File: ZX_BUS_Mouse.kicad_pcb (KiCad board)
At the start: 2 copper layers, 99.1 x 40 mm, 28 parts, among them J1 X1A, J2 X1B, J4 Mini-DIN-6, J5 Conn_02x03_Odd_Even ISP, J6 Conn_01x04 Debug, J7 Conn_02x05_Odd_Even JTAG, U1 ATmega8A-A, U2 EPM3032ALC44, U3 AMS1117-3.3

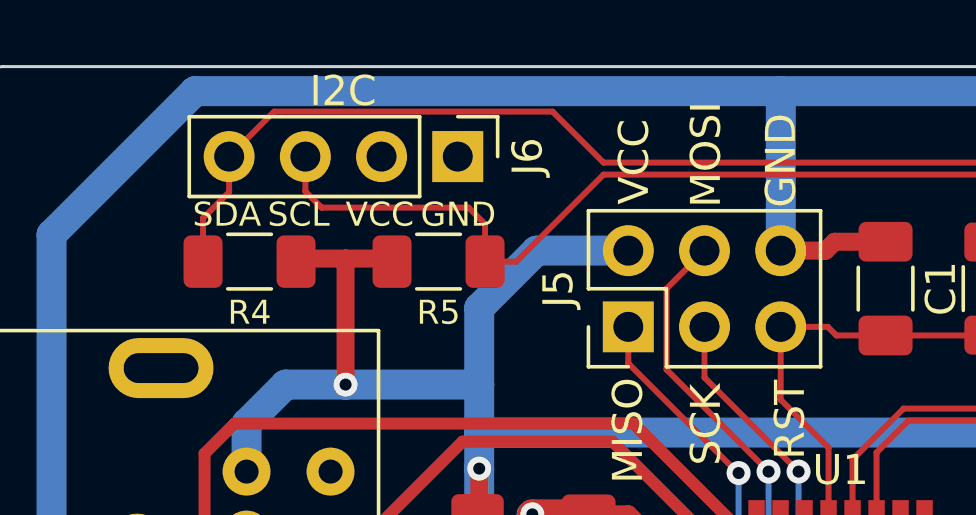
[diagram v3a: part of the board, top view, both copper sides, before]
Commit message: Connect I2C to VCC and GND.
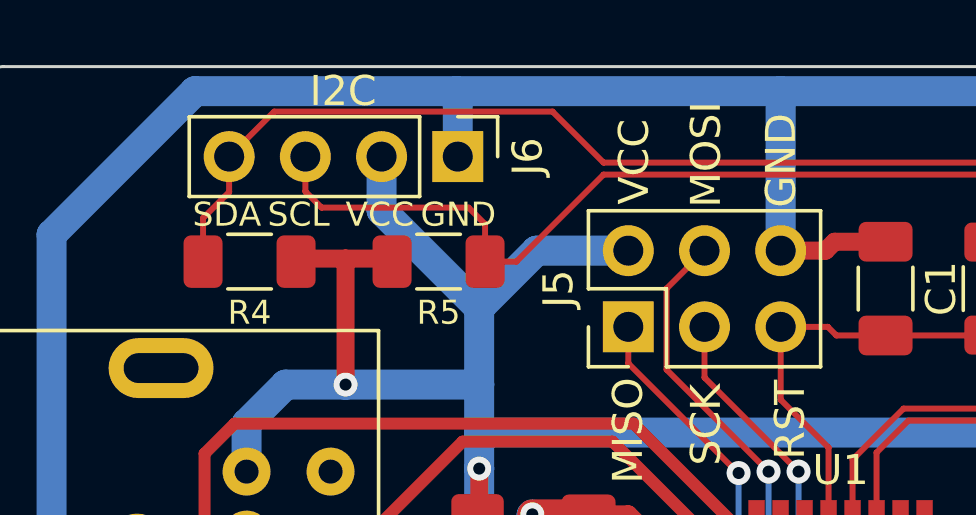
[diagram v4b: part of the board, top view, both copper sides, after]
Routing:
- net VCC: track 138.9 -> 145.3 mm
- net GND: track 497.9 -> 500.0 mm
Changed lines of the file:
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@@
   (via (at 115.2 138.2) (size 0.8) (drill 0.4) (layers "F.Cu" "B.Cu") (net 3))
   (segment (start 63.1 138.2) (end 135 138.2) (width 1) (layer "B.Cu") (net 3))
+  (segment (start 58.34 112.9) (end 58.34 110.75875) (width 1) (layer "B.Cu") (net 3))
   (segment (start 69.105 116.035) (end 69.105 110.72375) (width 1) (layer "B.Cu") (net 3))
   (segment (start 46.5 130.2) (end 51.3 130.2) (width 1) (layer "B.Cu") (net 3))
@@
   (segment (start 69.105 110.72375) (end 69.1 110.71875) (width 1) (layer "B.Cu") (net 3))
   (segment (start 115.18125 135.31875) (end 115.2 135.3) (width 0.6) (layer "B.Cu") (net 3))
+  (segment (start 58.3 110.71875) (end 49.58125 110.71875) (width 1) (layer "B.Cu") (net 3))
   (segment (start 112.4625 134.14125) (end 111.03 132.70875) (width 0.6) (layer "B.Cu") (net 3))
   (segment (start 100.8 130.48125) (end 102.01875 130.48125) (width 0.6) (layer "B.Cu") (net 3))
+  (segment (start 69.1 110.71875) (end 58.3 110.71875) (width 1) (layer "B.Cu") (net 3))
   (segment (start 97.3 132.5) (end 97.3 121.6) (width 1) (layer "B.Cu") (net 3))
   (segment (start 60.8 135.9) (end 63.1 138.2) (width 1) (layer "B.Cu") (net 3))
@@
   (segment (start 116.11 114.01) (end 116.11 114.92875) (width 0.6) (layer "B.Cu") (net 3))
   (segment (start 115.7625 113.6625) (end 116.11 114.01) (width 0.6) (layer "B.Cu") (net 3))
+  (segment (start 58.34 110.75875) (end 58.3 110.71875) (width 1) (layer "B.Cu") (net 3))
   (segment (start 136.31875 110.71875) (end 69.1 110.71875) (width 1) (layer "B.Cu") (net 3))
   (segment (start 122.41875 112.31875) (end 115.7625 112.31875) (width 1) (layer "B.Cu") (net 3))
@@
   (segment (start 112.4625 135.31875) (end 115.18125 135.31875) (width 1) (layer "B.Cu") (net 3))
   (segment (start 137 129.41875) (end 137.6 128.81875) (width 1) (layer "B.Cu") (net 3))
-  (segment (start 69.1 110.71875) (end 49.58125 110.71875) (width 1) (layer "B.Cu") (net 3))
   (segment (start 60.8 124.85) (end 60.8 130.8) (width 1) (layer "B.Cu") (net 3))
   (segment (start 93 118.56875) (end 92.8 118.76875) (width 1) (layer "B.Cu") (net 3))
@@
   (segment (start 81.65 113.55) (end 79.95 115.25) (width 1) (layer "B.Cu") (net 57))
   (segment (start 79.95 122.35) (end 83.3 125.7) (width 1) (layer "B.Cu") (net 57))
+  (segment (start 55.8 114.69) (end 59.055 117.945) (width 1) (layer "B.Cu") (net 57))
   (segment (start 83.3 130.565688) (end 83.282844 130.582844) (width 1) (layer "B.Cu") (net 57))
+  (segment (start 55.8 112.9) (end 55.8 114.69) (width 1) (layer "B.Cu") (net 57))
   (segment (start 64.025 116.035) (end 60.965 116.035) (width 1) (layer "B.Cu") (net 57))
   (segment (start 54.6 120.5) (end 52.6 120.5) (width 1) (layer "B.Cu") (net 57))

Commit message: Add labels to PCB.
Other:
- board text added: "JTAG"
- board text added: "ZX BUS Kempston Mouse Controller"
- board text added: "github.com/proboterror/ZX_BUS_Mouse"
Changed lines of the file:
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@@
     (effects (font (size 1 0.9) (thickness 0.15)) (justify mirror))
+  )
+  (gr_text "ZX BUS Kempston Mouse Controller" (at 94.9 125.5) (layer "B.SilkS")
+    (effects (font (size 1.2 1.2) (thickness 0.17)) (justify left bottom mirror))
   )
   (gr_text "*HLT/" (at 89.535 139.065 90) (layer "B.SilkS")
@@
   (gr_text "*RFSH/" (at 114.935 139.065 90) (layer "B.SilkS")
     (effects (font (size 1 0.7) (thickness 0.15)) (justify mirror))
+  )
+  (gr_text "github.com/proboterror/ZX_BUS_Mouse" (at 93.4 127.4) (layer "B.SilkS")
+    (effects (font (size 1 1) (thickness 0.15)) (justify left bottom mirror))
   )
   (gr_text "*D7" (at 59.055 139.065 90) (layer "B.SilkS")
@@
     (effects (font (size 1 0.7) (thickness 0.15)))
   )
+  (gr_text "JTAG" (at 134.7 134.3) (layer "F.SilkS")
+    (effects (font (size 1 1) (thickness 0.15)) (justify left bottom))
+  )
   (gr_text "SCL" (at 52 115.3) (layer "F.SilkS")

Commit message: Arrange resistors references.
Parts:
- renumbered R6 to R4, R7 to R5, R8 to R6, R9 to R7, R4 to R8, R5 to R9
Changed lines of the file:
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@@
     (property "ki_keywords" "R res resistor")
     (attr smd)
-    (fp_text reference "R6" (at 0 -1.6) (layer "F.SilkS")
+    (fp_text reference "R4" (at 0 -1.6) (layer "F.SilkS")
         (effects (font (size 1 1) (thickness 0.15)))
     )
@@
     (property "ki_keywords" "R res resistor")
     (attr smd)
-    (fp_text reference "R4" (at 0 -1.7) (layer "F.SilkS")
+    (fp_text reference "R8" (at 0 -1.7) (layer "F.SilkS")
         (effects (font (size 0.8 0.8) (thickness 0.1)))
     )
@@
     (property "ki_keywords" "R res resistor")
     (attr smd)
-    (fp_text reference "R8" (at 0 -1.71875) (layer "F.SilkS")
+    (fp_text reference "R6" (at 0 -1.71875) (layer "F.SilkS")
         (effects (font (size 1 1) (thickness 0.15)))
     )
@@
     (property "ki_keywords" "R res resistor")
     (attr smd)
-    (fp_text reference "R5" (at 0 1.7) (layer "F.SilkS")
+    (fp_text reference "R9" (at 0 1.7) (layer "F.SilkS")
         (effects (font (size 0.8 0.8) (thickness 0.1)))
     )
@@
     (property "ki_keywords" "R res resistor")
     (attr smd)
-    (fp_text reference "R9" (at 0 -1.6) (layer "F.SilkS")
+    (fp_text reference "R7" (at 0 -1.6) (layer "F.SilkS")
         (effects (font (size 1 1) (thickness 0.15)))
     )
@@
     (property "ki_keywords" "R res resistor")
     (attr smd)
-    (fp_text reference "R7" (at 0 -1.61875) (layer "F.SilkS")
-        (effects (font (size 1 1) (thickness 0.15)))
-    )
+    (fp_text reference "R5" (at 0 -1.61875) (layer "F.SilkS")
+        (effects (font (size 1 1) (thickness 0.15)))
+    )
